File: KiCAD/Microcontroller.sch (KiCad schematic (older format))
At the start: 172 parts, among them J4 0.1\" HDR, SW1 JS202011SCQN, SW2 EVQ-Q2B03W, U2 STM32H743ZITx, U3 USB3300-EZK, Y1 48MHz, Y2 24MHz

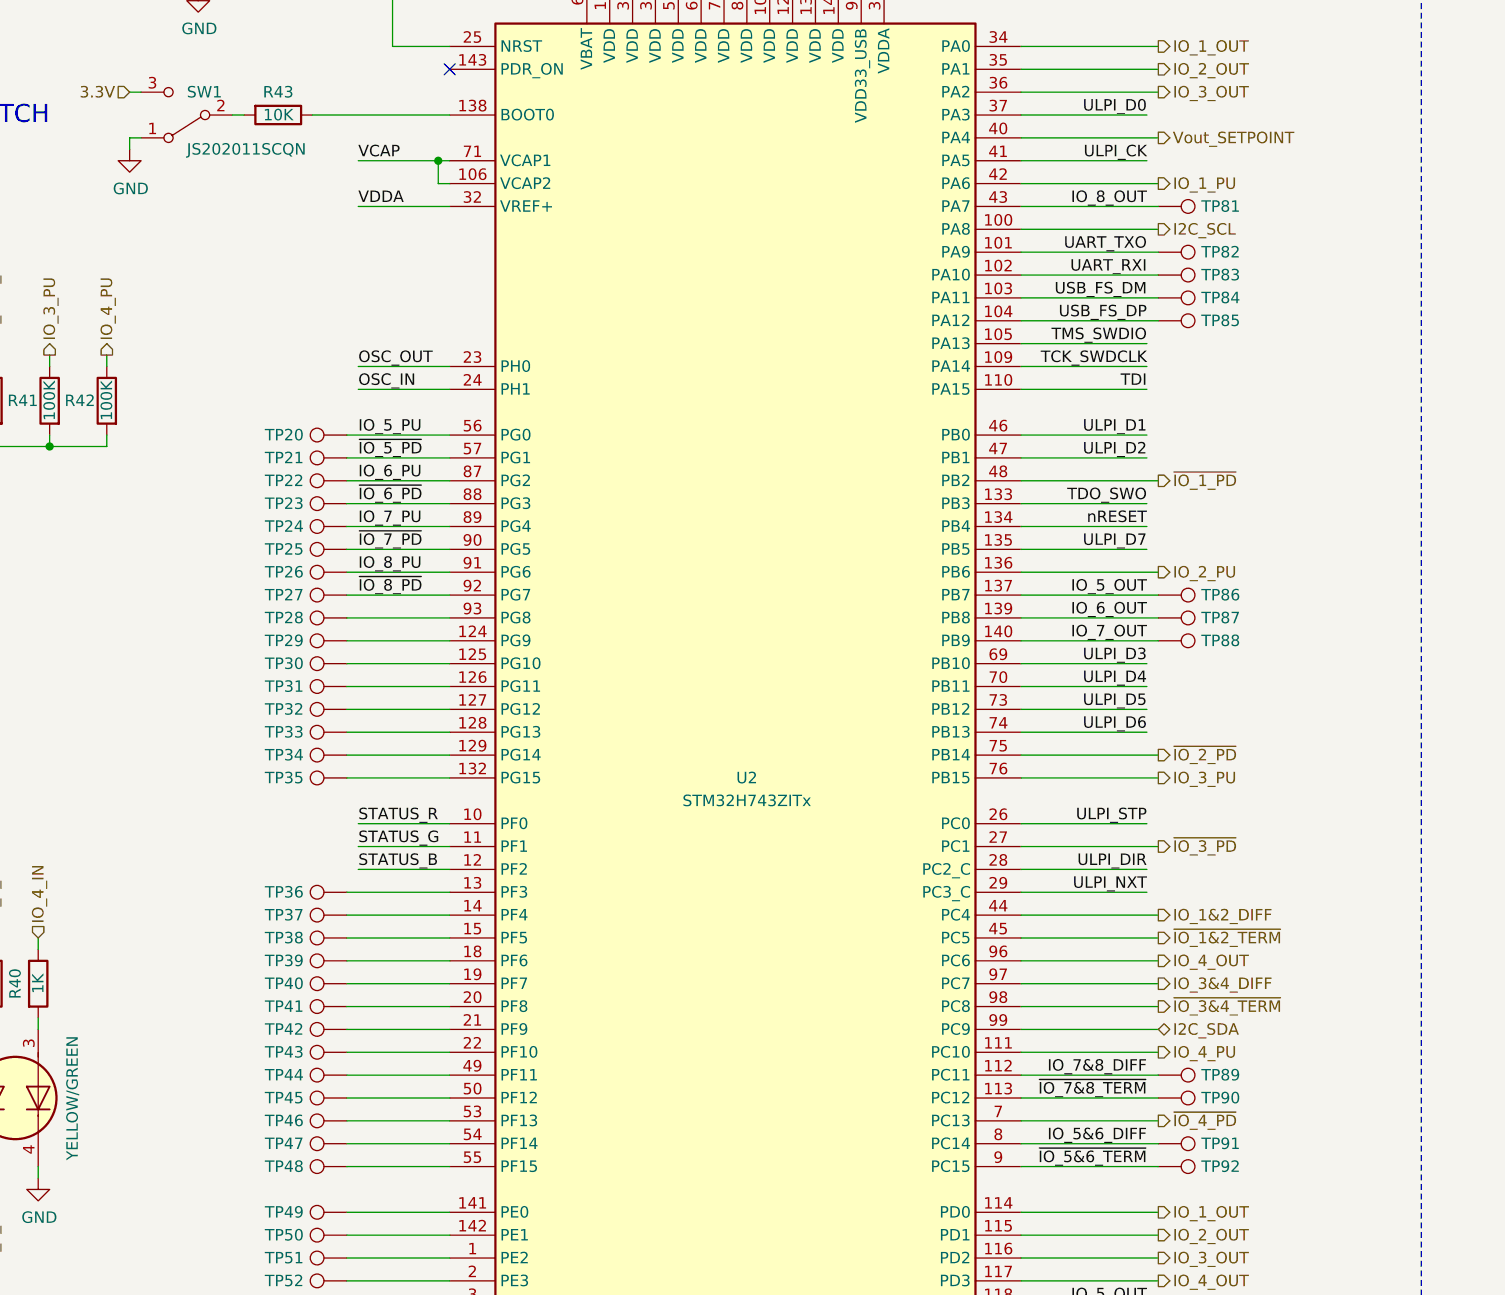
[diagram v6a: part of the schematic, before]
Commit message: Update microcontroller pin assignments
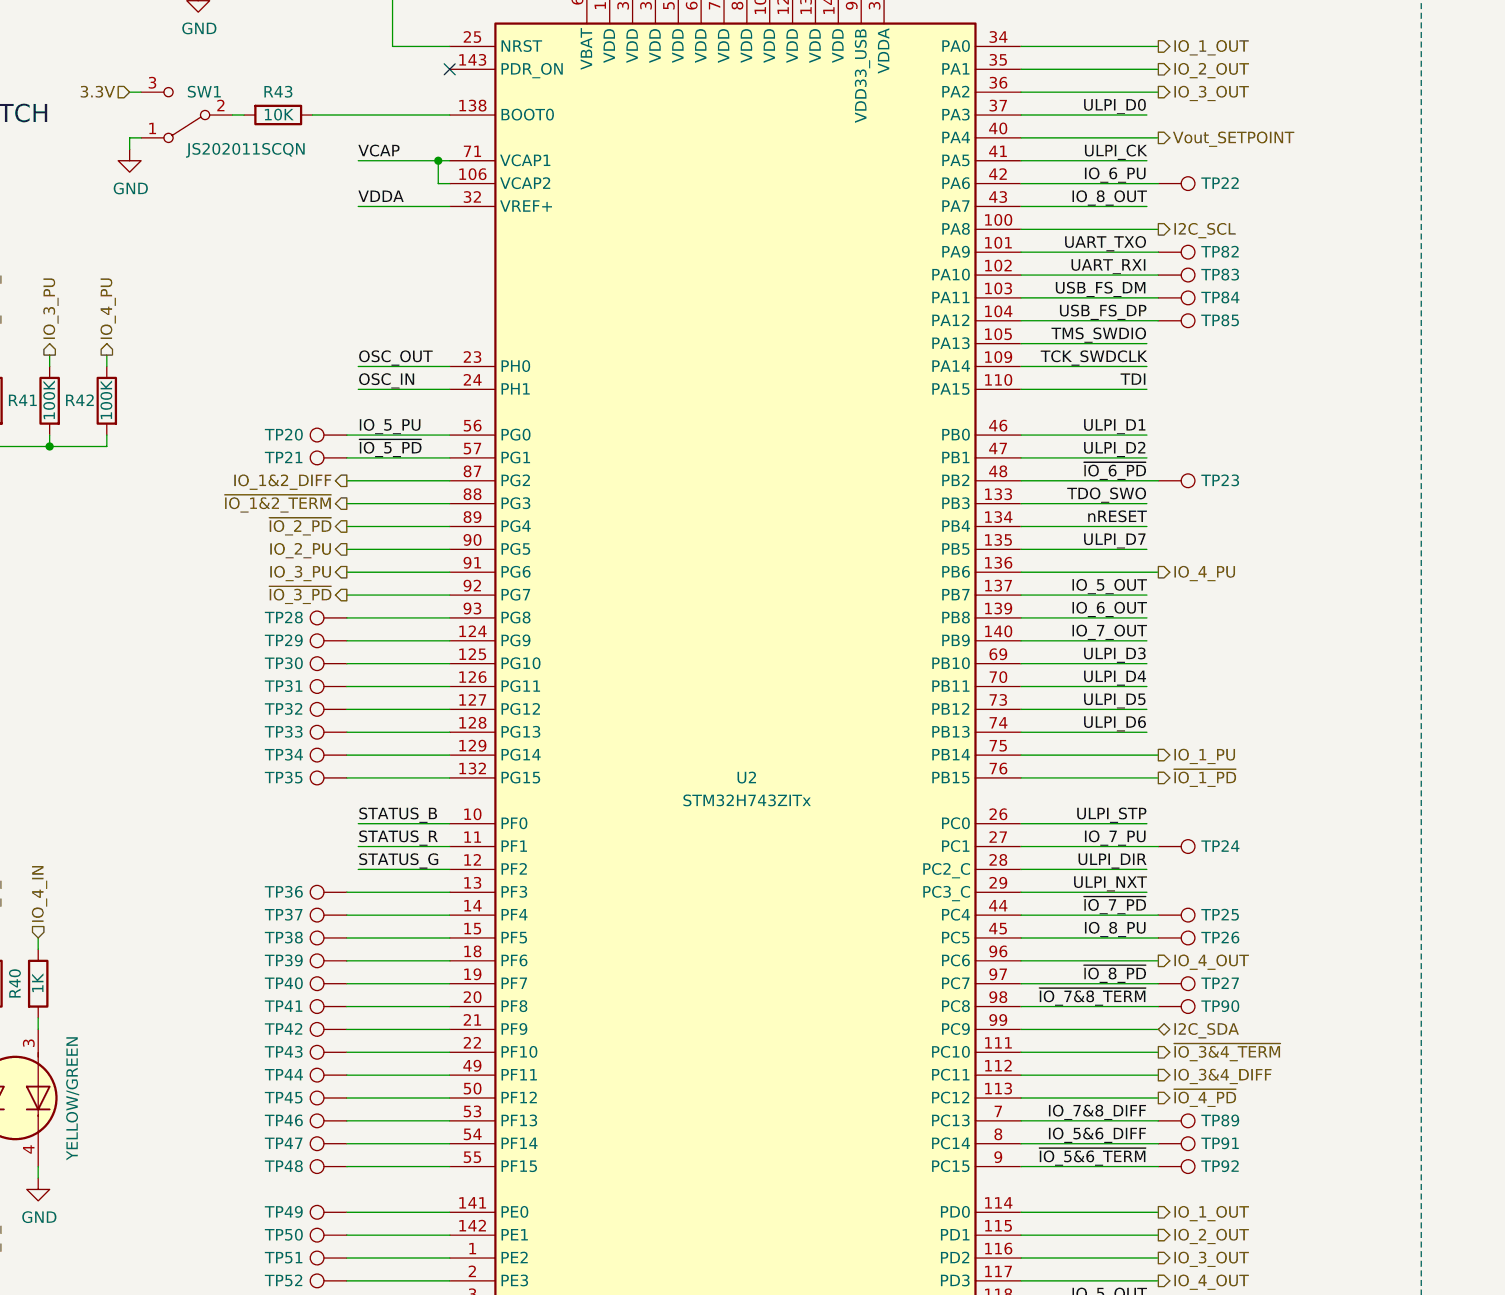
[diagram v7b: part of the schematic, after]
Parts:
- removed TP81: OUT8, TestPoint:TestPoint_Pad_D1.0mm, symbol Connector:TestPoint
- removed TP86: OUT5, TestPoint:TestPoint_Pad_D1.0mm, symbol Connector:TestPoint
- removed TP87: OUT6, TestPoint:TestPoint_Pad_D1.0mm, symbol Connector:TestPoint
- removed TP88: OUT7, TestPoint:TestPoint_Pad_D1.0mm, symbol Connector:TestPoint
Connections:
- net IO_1&2_DIFF: now also U2.87 (PG2); no longer U2.44 (PC4)
- net IO_1_PU: now also U2.75 (PB14); no longer U2.42 (PA6)
- net IO_2_PU: now also U2.90 (PG5); no longer U2.136 (PB6)
- net IO_3&4_DIFF: now also U2.112 (PC11); no longer U2.97 (PC7)
- net IO_3_PU: now also U2.91 (PG6); no longer U2.76 (PB15)
- net IO_4_PU: now also U2.136 (PB6); no longer U2.111 (PC10)
- net IO_6_PU: now also U2.42 (PA6); no longer U2.87 (PG2)
- net IO_7&8_DIFF: now also U2.7 (PC13); no longer U2.112 (PC11)
- net IO_7_PU: now also U2.27 (PC1); no longer U2.89 (PG4)
- net IO_8_PU: now also U2.45 (PC5); no longer U2.91 (PG6)
- net STATUS_B: now also U2.10 (PF0); no longer U2.12 (PF2)
- net STATUS_G: now also U2.12 (PF2); no longer U2.11 (PF1)
- net STATUS_R: now also U2.11 (PF1); no longer U2.10 (PF0)
- net ~IO_1&2_TERM: now also U2.88 (PG3); no longer U2.45 (PC5)
- net ~IO_1_PD: now also U2.76 (PB15); no longer U2.48 (PB2)
- net ~IO_2_PD: now also U2.89 (PG4); no longer U2.75 (PB14)
- net ~IO_3&4_TERM: now also U2.111 (PC10); no longer U2.98 (PC8)
- net ~IO_3_PD: now also U2.92 (PG7); no longer U2.27 (PC1)
- net ~IO_4_PD: now also U2.113 (PC12); no longer U2.7 (PC13)
- net ~IO_6_PD: now also U2.48 (PB2); no longer U2.88 (PG3)
- net ~IO_7&8_TERM: now also U2.98 (PC8); no longer U2.113 (PC12)
- net ~IO_7_PD: now also U2.44 (PC4); no longer U2.90 (PG5)
- net ~IO_8_PD: now also U2.97 (PC7); no longer U2.92 (PG7)
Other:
- moved on the sheet: TP22, TP23, TP24, TP25, TP26, TP27, TP89, TP90
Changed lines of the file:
@@
 Sheet 2 10
 Title "MICROCONTROLLER SUBSYSTEM"
-Date "2020-02-10"
+Date "2020-02-13"
 Rev "A"
 Comp "THE UNIVERSITY OF AKRON"
@@
 Text HLabel 7600 8300 0    50   Input ~ 0
 IO_1_IN
-Text HLabel 11150 3000 2    50   Output ~ 0
+Text HLabel 11150 5500 2    50   Output ~ 0
 IO_1_PU
-Text HLabel 11150 4300 2    50   Output ~ 0
+Text HLabel 11150 5600 2    50   Output ~ 0
 ~IO_1_PD
 Text HLabel 7600 8400 0    50   Input ~ 0
 IO_2_IN
-Text HLabel 11150 4700 2    50   Output ~ 0
+Text HLabel 7600 4600 0    50   Output ~ 0
 IO_2_PU
-Text HLabel 11150 5500 2    50   Output ~ 0
+Text HLabel 7600 4500 0    50   Output ~ 0
 ~IO_2_PD
 Text HLabel 7600 8500 0    50   Input ~ 0
 IO_3_IN
-Text HLabel 11150 5600 2    50   Output ~ 0
+Text HLabel 7600 4700 0    50   Output ~ 0
 IO_3_PU
-Text HLabel 11150 5900 2    50   Output ~ 0
+Text HLabel 7600 4800 0    50   Output ~ 0
 ~IO_3_PD
 Text HLabel 11150 6400 2    50   Output ~ 0
@@
 Text HLabel 7600 8600 0    50   Input ~ 0
 IO_4_IN
+Text HLabel 11150 4700 2    50   Output ~ 0
+IO_4_PU
+Text HLabel 11150 7000 2    50   Output ~ 0
+~IO_4_PD
+Text HLabel 11150 6900 2    50   Output ~ 0
+IO_3&4_DIFF
 Text HLabel 11150 6800 2    50   Output ~ 0
-IO_4_PU
-Text HLabel 11150 7100 2    50   Output ~ 0
-~IO_4_PD
-Text HLabel 11150 6500 2    50   Output ~ 0
-IO_3&4_DIFF
-Text HLabel 11150 6600 2    50   Output ~ 0
 ~IO_3&4_TERM
 $Comp
@@
 Wire Wire Line
 	11150 3000 10550 3000
-Text HLabel 11150 6200 2    50   Output ~ 0
+Text HLabel 7600 4300 0    50   Output ~ 0
 IO_1&2_DIFF
 Wire Wire Line
 	11150 6200 10550 6200
-Text HLabel 11150 6300 2    50   Output ~ 0
+Text HLabel 7600 4400 0    50   Output ~ 0
 ~IO_1&2_TERM
 Wire Wire Line
@@
 Text Label 11100 5000 2    50   ~ 0
 IO_7_OUT
-$Comp
-L Connector:TestPoint TP86
-U 1 1 60059113
-P 11150 4800
-F 0 "TP86" V 11150 4988 50  0000 L CNN
-F 1 "OUT5" V 11195 4988 50  0001 L CNN
-F 2 "TestPoint:TestPoint_Pad_D1.0mm" H 11350 4800 50  0001 C CNN
-F 3 "~" H 11350 4800 50  0001 C CNN
-	1    11150 4800
-	0    1    1    0
-$EndComp
-$Comp
-L Connector:TestPoint TP87
-U 1 1 6005911D
-P 11150 4900
-F 0 "TP87" V 11150 5088 50  0000 L CNN
-F 1 "OUT6" V 11195 5088 50  0001 L CNN
-F 2 "TestPoint:TestPoint_Pad_D1.0mm" H 11350 4900 50  0001 C CNN
-F 3 "~" H 11350 4900 50  0001 C CNN
-	1    11150 4900
-	0    1    1    0
-$EndComp
-$Comp
-L Connector:TestPoint TP88
-U 1 1 60059127
-P 11150 5000
-F 0 "TP88" V 11150 5188 50  0000 L CNN
-F 1 "OUT7" V 11195 5188 50  0001 L CNN
-F 2 "TestPoint:TestPoint_Pad_D1.0mm" H 11350 5000 50  0001 C CNN
-F 3 "~" H 11350 5000 50  0001 C CNN
-	1    11150 5000
-	0    1    1    0
-$EndComp
-Wire Wire Line
-	11150 4800 10550 4800
-Wire Wire Line
-	10550 4900 11150 4900
-Wire Wire Line
-	11150 5000 10550 5000
+Wire Wire Line
+	11100 4800 10550 4800
+Wire Wire Line
+	10550 4900 11100 4900
+Wire Wire Line
+	11100 5000 10550 5000
 Text HLabel 4300 3750 1    50   Output ~ 0
 IO_1&2_DIFF
@@
 Wire Wire Line
 	4300 5000 4300 4950
-Text Label 11100 6900 2    50   ~ 0
+Text Label 11100 7100 2    50   ~ 0
 IO_7&8_DIFF
-Text Label 11100 7000 2    50   ~ 0
+Text Label 11100 6600 2    50   ~ 0
 ~IO_7&8_TERM
 $Comp
 L Connector:TestPoint TP89
 U 1 1 601A2BB6
-P 11150 6900
-F 0 "TP89" V 11150 7088 50  0000 L CNN
-F 1 "DIFF78" V 11195 7088 50  0001 L CNN
-F 2 "TestPoint:TestPoint_Pad_D1.0mm" H 11350 6900 50  0001 C CNN
-F 3 "~" H 11350 6900 50  0001 C CNN
-	1    11150 6900
+P 11150 7100
+F 0 "TP89" V 11150 7288 50  0000 L CNN
+F 1 "DIFF78" V 11195 7288 50  0001 L CNN
+F 2 "TestPoint:TestPoint_Pad_D1.0mm" H 11350 7100 50  0001 C CNN
+F 3 "~" H 11350 7100 50  0001 C CNN
+	1    11150 7100
 	0    1    1    0
 $EndComp
@@
 L Connector:TestPoint TP90
 U 1 1 601A2E5C
-P 11150 7000
-F 0 "TP90" V 11150 7188 50  0000 L CNN
-F 1 "TERM78" V 11195 7188 50  0001 L CNN
-F 2 "TestPoint:TestPoint_Pad_D1.0mm" H 11350 7000 50  0001 C CNN
-F 3 "~" H 11350 7000 50  0001 C CNN
-	1    11150 7000
+P 11150 6600
+F 0 "TP90" V 11150 6788 50  0000 L CNN
+F 1 "TERM78" V 11195 6788 50  0001 L CNN
+F 2 "TestPoint:TestPoint_Pad_D1.0mm" H 11350 6600 50  0001 C CNN
+F 3 "~" H 11350 6600 50  0001 C CNN
+	1    11150 6600
 	0    1    1    0
 $EndComp
@@
 L Connector:TestPoint TP22
 U 1 1 60B92904
-P 7600 4300
-F 0 "TP22" V 7600 4488 50  0000 L CNN
-F 1 "PU6" V 7645 4488 50  0001 L CNN
-F 2 "TestPoint:TestPoint_Pad_D1.0mm" H 7800 4300 50  0001 C CNN
-F 3 "~" H 7800 4300 50  0001 C CNN
-	1    7600 4300
-	0    -1   1    0
+P 11150 3000
+F 0 "TP22" V 11150 3188 50  0000 L CNN
+F 1 "PU6" V 11195 3188 50  0001 L CNN
+F 2 "TestPoint:TestPoint_Pad_D1.0mm" H 11350 3000 50  0001 C CNN
+F 3 "~" H 11350 3000 50  0001 C CNN
+	1    11150 3000
+	0    1    -1   0
 $EndComp
 $Comp
 L Connector:TestPoint TP23
 U 1 1 60B9290E
-P 7600 4400
-F 0 "TP23" V 7600 4588 50  0000 L CNN
-F 1 "PD6" V 7645 4588 50  0001 L CNN
-F 2 "TestPoint:TestPoint_Pad_D1.0mm" H 7800 4400 50  0001 C CNN
-F 3 "~" H 7800 4400 50  0001 C CNN
-	1    7600 4400
-	0    -1   1    0
+P 11150 4300
+F 0 "TP23" V 11150 4488 50  0000 L CNN
+F 1 "PD6" V 11195 4488 50  0001 L CNN
+F 2 "TestPoint:TestPoint_Pad_D1.0mm" H 11350 4300 50  0001 C CNN
+F 3 "~" H 11350 4300 50  0001 C CNN
+	1    11150 4300
+	0    1    -1   0
 $EndComp
 $Comp
 L Connector:TestPoint TP24
 U 1 1 60B92918
-P 7600 4500
-F 0 "TP24" V 7600 4688 50  0000 L CNN
-F 1 "PU7" V 7645 4688 50  0001 L CNN
-F 2 "TestPoint:TestPoint_Pad_D1.0mm" H 7800 4500 50  0001 C CNN
-F 3 "~" H 7800 4500 50  0001 C CNN
-	1    7600 4500
-	0    -1   1    0
+P 11150 5900
+F 0 "TP24" V 11150 6088 50  0000 L CNN
+F 1 "PU7" V 11195 6088 50  0001 L CNN
+F 2 "TestPoint:TestPoint_Pad_D1.0mm" H 11350 5900 50  0001 C CNN
+F 3 "~" H 11350 5900 50  0001 C CNN
+	1    11150 5900
+	0    1    -1   0
 $EndComp
 $Comp
 L Connector:TestPoint TP25
 U 1 1 60B92922
-P 7600 4600
-F 0 "TP25" V 7600 4788 50  0000 L CNN
-F 1 "PD7" V 7645 4788 50  0001 L CNN
-F 2 "TestPoint:TestPoint_Pad_D1.0mm" H 7800 4600 50  0001 C CNN
-F 3 "~" H 7800 4600 50  0001 C CNN
-	1    7600 4600
-	0    -1   1    0
+P 11150 6200
+F 0 "TP25" V 11150 6388 50  0000 L CNN
+F 1 "PD7" V 11195 6388 50  0001 L CNN
+F 2 "TestPoint:TestPoint_Pad_D1.0mm" H 11350 6200 50  0001 C CNN
+F 3 "~" H 11350 6200 50  0001 C CNN
+	1    11150 6200
+	0    1    -1   0
 $EndComp
 $Comp
 L Connector:TestPoint TP26
 U 1 1 60B9292C
-P 7600 4700
-F 0 "TP26" V 7600 4888 50  0000 L CNN
-F 1 "PU8" V 7645 4888 50  0001 L CNN
-F 2 "TestPoint:TestPoint_Pad_D1.0mm" H 7800 4700 50  0001 C CNN
-F 3 "~" H 7800 4700 50  0001 C CNN
-	1    7600 4700
-	0    -1   1    0
+P 11150 6300
+F 0 "TP26" V 11150 6488 50  0000 L CNN
+F 1 "PU8" V 11195 6488 50  0001 L CNN
+F 2 "TestPoint:TestPoint_Pad_D1.0mm" H 11350 6300 50  0001 C CNN
+F 3 "~" H 11350 6300 50  0001 C CNN
+	1    11150 6300
+	0    1    -1   0
 $EndComp
 $Comp
 L Connector:TestPoint TP27
 U 1 1 60B92936
-P 7600 4800
-F 0 "TP27" V 7600 4988 50  0000 L CNN
-F 1 "PD8" V 7645 4988 50  0001 L CNN
-F 2 "TestPoint:TestPoint_Pad_D1.0mm" H 7800 4800 50  0001 C CNN
-F 3 "~" H 7800 4800 50  0001 C CNN
-	1    7600 4800
-	0    -1   1    0
+P 11150 6500
+F 0 "TP27" V 11150 6688 50  0000 L CNN
+F 1 "PD8" V 11195 6688 50  0001 L CNN
+F 2 "TestPoint:TestPoint_Pad_D1.0mm" H 11350 6500 50  0001 C CNN
+F 3 "~" H 11350 6500 50  0001 C CNN
+	1    11150 6500
+	0    1    -1   0
 $EndComp
 Wire Wire Line
@@
 IO_8_OUT
 Wire Wire Line
-	10550 3100 11150 3100
-$Comp
-L Connector:TestPoint TP81
-U 1 1 612699DD
-P 11150 3100
-F 0 "TP81" V 11150 3288 50  0000 L CNN
-F 1 "OUT8" V 11195 3288 50  0001 L CNN
-F 2 "TestPoint:TestPoint_Pad_D1.0mm" H 11350 3100 50  0001 C CNN
-F 3 "~" H 11350 3100 50  0001 C CNN
-	1    11150 3100
-	0    1    1    0
-$EndComp
+	10550 3100 11100 3100
 Wire Wire Line
 	11150 3500 10550 3500
@@
 Text Label 7650 4200 0    50   ~ 0
 ~IO_5_PD
-Text Label 7650 4300 0    50   ~ 0
+Text Label 11100 3000 2    50   ~ 0
 IO_6_PU
-Text Label 7650 4400 0    50   ~ 0
+Text Label 11100 4300 2    50   ~ 0
 ~IO_6_PD
-Text Label 7650 4500 0    50   ~ 0
+Text Label 11100 5900 2    50   ~ 0
 IO_7_PU
-Text Label 7650 4600 0    50   ~ 0
+Text Label 11100 6200 2    50   ~ 0
 ~IO_7_PD
-Text Label 7650 4700 0    50   ~ 0
+Text Label 11100 6300 2    50   ~ 0
 IO_8_PU
-Text Label 7650 4800 0    50   ~ 0
+Text Label 11100 6500 2    50   ~ 0
 ~IO_8_PD
 Wire Wire Line
@@
 Wire Wire Line
 	7650 5800 8050 5800
+Text Label 7650 5900 0    50   ~ 0
+STATUS_R
+Text Label 7650 6000 0    50   ~ 0
+STATUS_G
 Text Label 7650 5800 0    50   ~ 0
-STATUS_R
-Text Label 7650 5900 0    50   ~ 0
-STATUS_G
-Text Label 7650 6000 0    50   ~ 0
 STATUS_B
 Text Label 4500 8250 0    50   ~ 0
